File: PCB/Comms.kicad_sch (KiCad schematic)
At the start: 19 parts, among them J2 USB_In, J3 Trackpad, J4 OLED, U4 PMW3360DM-T2QU, U5 SRV05-4

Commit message: Rewording of readme. Added files for JLC PCBA. Changed USB C connector and moved it away from board.
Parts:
- C20: LCSC (none) -> C14663; LCSC part number C14663 -> (none)
- C93: LCSC (none) -> C19666; LCSC part number C19666 -> (none)
- C94: LCSC (none) -> C1525; LCSC part number C1525 -> (none)
- D64: LCSC (none) -> C193402; LCSC part number C193402 -> (none)
- D65, D66: LCSC (none) -> C8598; LCSC part number C8598 -> (none)
- F1: LCSC (none) -> C66453; LCSC part number C66453 -> (none)
- J2: footprint Honeydew:HRO-TYPE-C-31-M-13x -> Honeydew:HRO-TYPE-C-31-M-12; LCSC (none) -> C165948; LCSC part number C2848620 -> (none)
- J3: LCSC (none) -> C88360; LCSC part number C88360 -> (none)
- R10, R14: LCSC (none) -> C25744; LCSC part number C25744 -> (none)
- R11: LCSC (none) -> C25164; LCSC part number C25164 -> (none)
- R12, R13: LCSC (none) -> C25905; LCSC part number C25905 -> (none)
- R26: LCSC (none) -> C23138; LCSC part number C23138 -> (none)
- U4: now left out of the parts list
- U5: LCSC (none) -> C85364; LCSC part number C85364 -> (none)
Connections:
- net at J2.A5 (CC1): now also R13.2; no longer R12.2
- net at J2.B5 (CC2): now also R12.2; no longer R13.2
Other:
- moved on the sheet: R12, R13
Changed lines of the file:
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@@
-      (effects (font (size 1.27 1.27)) hide)
-    )
-    (property "LCSC part number" "C8598" (at 85.09 21.59 0)
       (effects (font (size 1.27 1.27)) hide)
     )
     (property "Description" "SOD-123 schottky" (at 85.09 21.59 0)
+      (effects (font (size 1.27 1.27)) hide)
+    )
+    (property "LCSC" "C8598" (at 85.09 21.59 0)
       (effects (font (size 1.27 1.27)) hide)
     )
@@
       (effects (font (size 1.27 1.27)) hide)
     )
-    (property "LCSC part number" "C88360" (at 116.84 83.82 0)
-      (effects (font (size 1.27 1.27)) hide)
-    )
     (property "Description" "12-pin FFC/FPC connector" (at 116.84 83.82 0)
+      (effects (font (size 1.27 1.27)) hide)
+    )
+    (property "LCSC" "C88360" (at 116.84 83.82 0)
       (effects (font (size 1.27 1.27)) hide)
     )
@@
       (effects (font (size 1.27 1.27)) hide)
     )
-    (property "LCSC part number" "C25744" (at 118.11 29.21 0)
+    (property "LCSC" "C25744" (at 118.11 29.21 0)
       (effects (font (size 1.27 1.27)) hide)
     )
@@
       (effects (font (size 1.27 1.27)) hide)
     )
-    (property "LCSC part number" "C14663" (at 24.13 67.31 0)
-      (effects (font (size 1.27 1.27)) hide)
-    )
     (property "Description" "0603 capacitor" (at 24.13 67.31 0)
+      (effects (font (size 1.27 1.27)) hide)
+    )
+    (property "LCSC" "C14663" (at 24.13 67.31 0)
       (effects (font (size 1.27 1.27)) hide)
     )
@@
       (effects (font (size 1.27 1.27)))
     )
-    (property "Footprint" "Honeydew:HRO-TYPE-C-31-M-13x" (at 30.48 36.83 0)
+    (property "Footprint" "Honeydew:HRO-TYPE-C-31-M-12" (at 30.48 36.83 0)
       (effects (font (size 1.27 1.27)) hide)
     )
@@
       (effects (font (size 1.27 1.27)) hide)
     )
-    (property "LCSC part number" "C2848620" (at 26.67 36.83 0)
-      (effects (font (size 1.27 1.27)) hide)
-    )
     (property "Description" "USB C 2.0 jack" (at 26.67 36.83 0)
       (effects (font (size 1.27 1.27)) hide)
     )
-    (property "LCSC" "" (at 26.67 36.83 0)
+    (property "LCSC" "C165948" (at 26.67 36.83 0)
       (effects (font (size 1.27 1.27)) hide)
     )
@@
       (effects (font (size 1.27 1.27)) hide)
     )
-    (property "LCSC part number" "C25164" (at 125.73 29.21 0)
-      (effects (font (size 1.27 1.27)) hide)
-    )
     (property "Description" "0402 resistor" (at 125.73 29.21 0)
       (effects (font (size 1.27 1.27)) hide)
     )
+    (property "LCSC" "C25164" (at 125.73 29.21 0)
+      (effects (font (size 1.27 1.27)) hide)
+    )
     (pin "1")
     (pin "2")
@@
   )
   (symbol (lib_name "PMW3360DM-T2QU_1") (lib_id "Ogen:PMW3360DM-T2QU") (at 140.97 39.37 0) (unit 1)
-    (in_bom yes) (on_board yes) (dnp no) (fields_autoplaced)
+    (in_bom no) (on_board yes) (dnp no) (fields_autoplaced)
     (property "Reference" "U4" (at 152.1402 54.61 0)
       (effects (font (size 1.27 1.27)))
@@
     )
     (property "Description" "Optical sensor" (at 140.97 39.37 0)
+      (effects (font (size 1.27 1.27)) hide)
+    )
+    (property "LCSC" "" (at 140.97 39.37 0)
       (effects (font (size 1.27 1.27)) hide)
     )
@@
       (effects (font (size 1.27 1.27)) hide)
     )
-    (property "LCSC part number" "C19666" (at 148.59 19.05 0)
-      (effects (font (size 1.27 1.27)) hide)
-    )
     (property "Description" "0603 capacitor" (at 148.59 19.05 0)
+      (effects (font (size 1.27 1.27)) hide)
+    )
+    (property "LCSC" "C19666" (at 148.59 19.05 0)
       (effects (font (size 1.27 1.27)) hide)
     )
@@
       (effects (font (size 1.27 1.27)) hide)
     )
-    (property "LCSC" "" (at 77.47 21.59 90)
-      (effects (font (size 1.27 1.27)) hide)
-    )
-    (property "LCSC part number" "C66453" (at 77.47 21.59 0)
-      (effects (font (size 1.27 1.27)) hide)
-    )
     (property "Description" "1206 fuse 1A" (at 77.47 21.59 0)
+      (effects (font (size 1.27 1.27)) hide)
+    )
+    (property "LCSC" "C66453" (at 77.47 21.59 0)
       (effects (font (size 1.27 1.27)) hide)
     )
@@
       (effects (font (size 1.27 1.27)) hide)
     )
-    (property "LCSC part number" "C85364" (at 72.39 44.45 0)
-      (effects (font (size 1.27 1.27)) hide)
-    )
     (property "Description" "SOT-26 ESD protector" (at 72.39 44.45 0)
       (effects (font (size 1.27 1.27)) hide)
     )
-    (property "LCSC" "" (at 72.39 44.45 0)
+    (property "LCSC" "C85364" (at 72.39 44.45 0)
       (effects (font (size 1.27 1.27)) hide)
     )
@@
       (effects (font (size 1.27 1.27)) hide)
     )
+    (property "LCSC" "" (at 166.37 35.56 0)
+      (effects (font (size 1.27 1.27)) hide)
+    )
     (pin "1")
     (pin "2")
@@
     )
   )
-  (symbol (lib_id "Device:R_Small") (at 46.99 26.67 270) (unit 1)
-    (in_bom yes) (on_board yes) (dnp no)
-    (property "Reference" "R12" (at 45.72 24.13 90)
+  (symbol (lib_id "Device:R_Small") (at 46.99 29.21 270) (mirror x) (unit 1)
+    (in_bom yes) (on_board yes) (dnp no)
+    (property "Reference" "R12" (at 45.72 31.75 90)
       (effects (font (size 1.27 1.27)) (justify right))
     )
-    (property "Value" "5k1" (at 48.26 24.13 90)
-      (effects (font (size 1.27 1.27)) (justify left))
-    )
-    (property "Footprint" "Resistor_SMD:R_0402_1005Metric" (at 46.99 26.67 0)
-      (effects (font (size 1.27 1.27)) hide)
-    )
-    (property "Datasheet" "~" (at 46.99 26.67 0)
-      (effects (font (size 1.27 1.27)) hide)
-    )
-    (property "LCSC part number" "C25905" (at 46.99 26.67 0)
-      (effects (font (size 1.27 1.27)) hide)
-    )
-    (property "Description" "0402 resistor" (at 46.99 26.67 0)
+    (property "Value" "5k1" (at 48.26 31.75 90)
+      (effects (font (size 1.27 1.27)) (justify left))
+    )
+    (property "Footprint" "Resistor_SMD:R_0402_1005Metric" (at 46.99 29.21 0)
+      (effects (font (size 1.27 1.27)) hide)
+    )
+    (property "Datasheet" "~" (at 46.99 29.21 0)
+      (effects (font (size 1.27 1.27)) hide)
+    )
+    (property "Description" "0402 resistor" (at 46.99 29.21 0)
+      (effects (font (size 1.27 1.27)) hide)
+    )
+    (property "LCSC" "C25905" (at 46.99 29.21 0)
       (effects (font (size 1.27 1.27)) hide)
     )
@@
       (effects (font (size 1.27 1.27)) hide)
     )
-    (property "LCSC part number" "C23138" (at 19.05 67.31 0)
-      (effects (font (size 1.27 1.27)) hide)
-    )
     (property "Description" "0603 resistor" (at 19.05 67.31 0)
+      (effects (font (size 1.27 1.27)) hide)
+    )
+    (property "LCSC" "C23138" (at 19.05 67.31 0)
       (effects (font (size 1.27 1.27)) hide)
     )
@@
       (effects (font (size 1.27 1.27)) hide)
     )
-    (property "LCSC part number" "C25744" (at 166.37 26.67 0)
+    (property "LCSC" "C25744" (at 166.37 26.67 0)
       (effects (font (size 1.27 1.27)) hide)
     )
@@
     )
   )
-  (symbol (lib_id "Device:R_Small") (at 46.99 29.21 270) (mirror x) (unit 1)
-    (in_bom yes) (on_board yes) (dnp no)
-    (property "Reference" "R13" (at 45.72 31.75 90)
+  (symbol (lib_id "Device:R_Small") (at 46.99 26.67 270) (unit 1)
+    (in_bom yes) (on_board yes) (dnp no)
+    (property "Reference" "R13" (at 45.72 24.13 90)
       (effects (font (size 1.27 1.27)) (justify right))
     )
-    (property "Value" "5k1" (at 48.26 31.75 90)
-      (effects (font (size 1.27 1.27)) (justify left))
-    )
-    (property "Footprint" "Resistor_SMD:R_0402_1005Metric" (at 46.99 29.21 0)
-      (effects (font (size 1.27 1.27)) hide)
-    )
-    (property "Datasheet" "~" (at 46.99 29.21 0)
-      (effects (font (size 1.27 1.27)) hide)
-    )
-    (property "LCSC part number" "C25905" (at 46.99 29.21 0)
-      (effects (font (size 1.27 1.27)) hide)
-    )
-    (property "Description" "0402 resistor" (at 46.99 29.21 0)
+    (property "Value" "5k1" (at 48.26 24.13 90)
+      (effects (font (size 1.27 1.27)) (justify left))
+    )
+    (property "Footprint" "Resistor_SMD:R_0402_1005Metric" (at 46.99 26.67 0)
+      (effects (font (size 1.27 1.27)) hide)
+    )
+    (property "Datasheet" "~" (at 46.99 26.67 0)
+      (effects (font (size 1.27 1.27)) hide)
+    )
+    (property "Description" "0402 resistor" (at 46.99 26.67 0)
+      (effects (font (size 1.27 1.27)) hide)
+    )
+    (property "LCSC" "C25905" (at 46.99 26.67 0)
       (effects (font (size 1.27 1.27)) hide)
     )
@@
       (effects (font (size 1.27 1.27)) hide)
     )
-    (property "LCSC part number" "C8598" (at 72.39 26.67 0)
-      (effects (font (size 1.27 1.27)) hide)
-    )
     (property "Description" "SOD-123 schottky" (at 72.39 26.67 0)
+      (effects (font (size 1.27 1.27)) hide)
+    )
+    (property "LCSC" "C8598" (at 72.39 26.67 0)
       (effects (font (size 1.27 1.27)) hide)
     )
@@
       (effects (font (size 1.27 1.27)) hide)
     )
-    (property "LCSC part number" "C193402" (at 57.15 26.67 0)
-      (effects (font (size 1.27 1.27)) hide)
-    )
     (property "Description" "SOD-123 TVS" (at 57.15 26.67 0)
+      (effects (font (size 1.27 1.27)) hide)
+    )
+    (property "LCSC" "C193402" (at 57.15 26.67 0)
       (effects (font (size 1.27 1.27)) hide)
     )
@@
       (effects (font (size 1.27 1.27)) hide)
     )
-    (property "LCSC part number" "C1525" (at 148.59 24.13 0)
-      (effects (font (size 1.27 1.27)) hide)
-    )
     (property "Description" "0402 capacitor" (at 148.59 24.13 0)
+      (effects (font (size 1.27 1.27)) hide)
+    )
+    (property "LCSC" "C1525" (at 148.59 24.13 0)
       (effects (font (size 1.27 1.27)) hide)
     )
@@
       (effects (font (size 1.27 1.27)) hide)
     )
-    (property "LCSC part number" "" (at 146.05 76.2 0)
-      (effects (font (size 1.27 1.27)) hide)
-    )
     (property "Description" "SSD1315 OLED" (at 146.05 76.2 0)
       (effects (font (size 1.27 1.27)) hide)
     )
+    (property "LCSC" "" (at 146.05 76.2 0)
+      (effects (font (size 1.27 1.27)) hide)
+    )

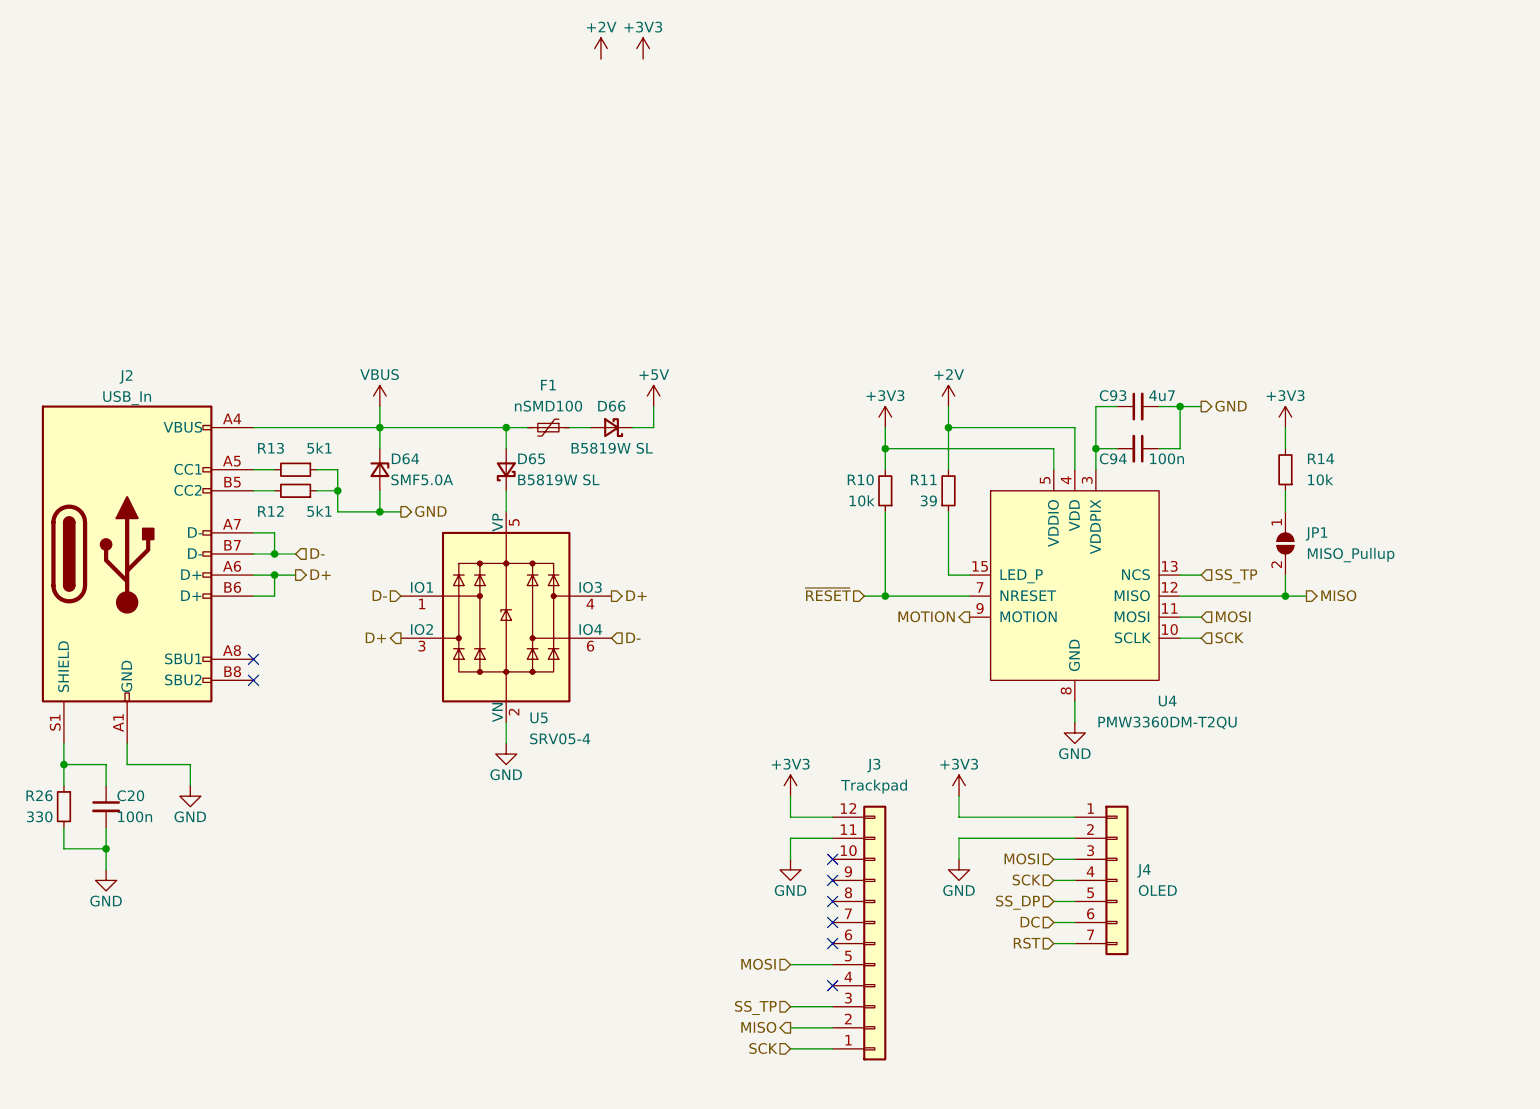
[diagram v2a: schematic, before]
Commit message: Added PH2.0 header for OLED. Changed plate to accommodate headers.
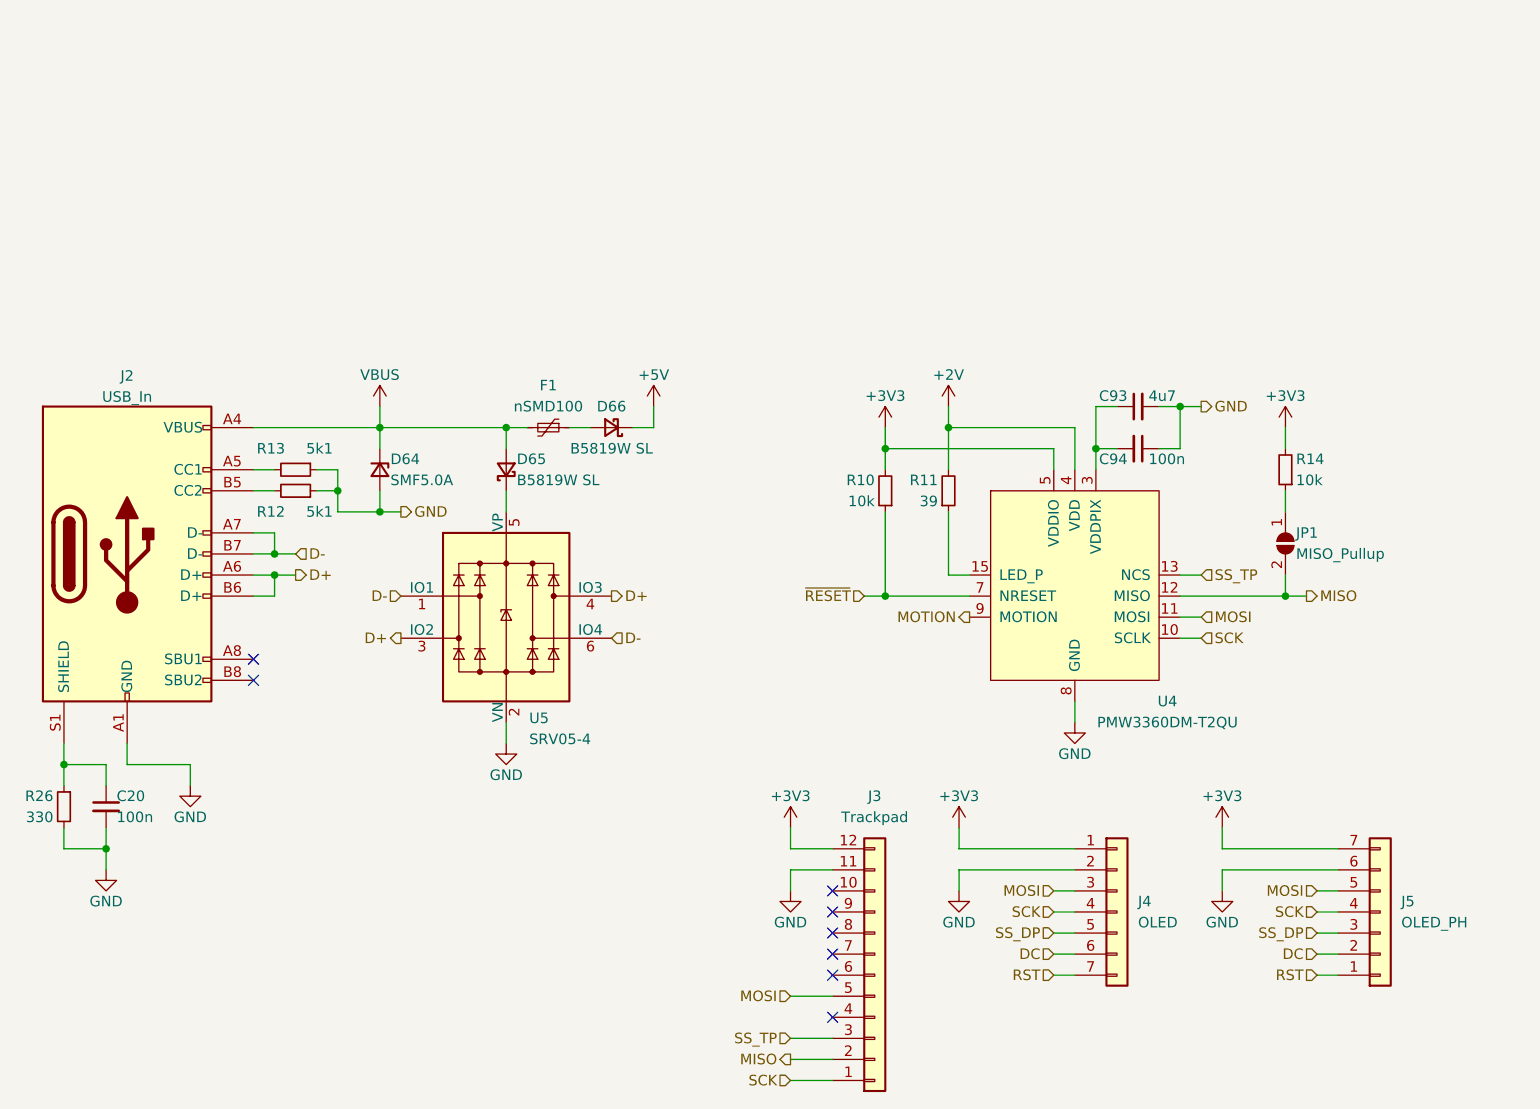
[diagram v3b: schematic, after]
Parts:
- added J5: OLED_PH, Connector_JST:JST_PH_S7B-PH-K_1x07_P2.00mm_Horizontal, symbol Connector_Generic:Conn_01x07
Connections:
- net +3V3: now also J5.7 (Pin_7)
- net DC: now also J5.2 (Pin_2)
- net GND: now also J5.6 (Pin_6)
- net MOSI: now also J5.5 (Pin_5)
- net RST: now also J5.1 (Pin_1)
- net SCK: now also J5.4 (Pin_4)
- net SS_DP: now also J5.3 (Pin_3)
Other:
- moved on the sheet: J3, J4

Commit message: V1.1 update.
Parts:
- removed C20: 100n, Capacitor_SMD:C_0603_1608Metric, symbol Device:C_Small
- removed R26: 330, Resistor_SMD:R_0603_1608Metric, symbol Device:R_Small
- added FB1: GZ2012D601TF, Inductor_SMD:L_0805_2012Metric, symbol Device:FerriteBead_Small
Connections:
- net GND: now also FB1.2
- net at J2.S1 (SHIELD): now also FB1.1

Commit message: Added level shifter to the RGB signal, just in case.
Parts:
- FB1: value GZ2012D601TF -> 60R@100MHz; footprint Inductor_SMD:L_0805_2012Metric -> Inductor_SMD:L_1206_3216Metric; LCSC C1017 -> C33600
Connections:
- net MOTION: now also J3.4 (Pin_4)
- net RST renamed RST_OLED
- net SS_DP renamed SS_OLED
- net SS_TP renamed SS_TB
- net ~{RESET} renamed ~{RST}_TB
- no-connect marks 8 -> 7
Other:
- moved on the sheet: J4, J5

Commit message: More V1.1 updates
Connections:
- net ~{RST}_TB is gone; now on net ~{RST}: R10.1, U4.7 (NRESET)
- net DC renamed DC_OLED
- net RST_OLED renamed ~{RST}
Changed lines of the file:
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@@
   (title_block
     (title "Honeydew unsplit ergonomic keyboard")
-    (date "2023-03-18")
+    (date "2023-03-31")
     (rev "V1.1")
   )
@@
     (stroke (width 0) (type default))
   )
-  (hierarchical_label "RST_OLED" (shape input) (at 175.26 87.63 180) (fields_autoplaced)
-    (effects (font (size 1.27 1.27)) (justify right))
-  )
   (hierarchical_label "D-" (shape input) (at 59.69 41.91 180) (fields_autoplaced)
     (effects (font (size 1.27 1.27)) (justify right))
@@
     (effects (font (size 1.27 1.27)) (justify right))
   )
+  (hierarchical_label "DC_OLED" (shape input) (at 175.26 85.09 180) (fields_autoplaced)
+    (effects (font (size 1.27 1.27)) (justify right))
+  )
   (hierarchical_label "SS_TB" (shape input) (at 106.68 95.25 180) (fields_autoplaced)
     (effects (font (size 1.27 1.27)) (justify right))
   )
-  (hierarchical_label "RST_OLED" (shape input) (at 140.97 87.63 180) (fields_autoplaced)
+  (hierarchical_label "~{RST}" (shape input) (at 140.97 87.63 180) (fields_autoplaced)
     (effects (font (size 1.27 1.27)) (justify right))
   )
@@
     (effects (font (size 1.27 1.27)) (justify left))
   )
+  (hierarchical_label "~{RST}" (shape input) (at 175.26 87.63 180) (fields_autoplaced)
+    (effects (font (size 1.27 1.27)) (justify right))
+  )
   (hierarchical_label "SS_OLED" (shape input) (at 175.26 82.55 180) (fields_autoplaced)
     (effects (font (size 1.27 1.27)) (justify right))
@@
     (effects (font (size 1.27 1.27)) (justify right))
   )
-  (hierarchical_label "DC" (shape input) (at 140.97 85.09 180) (fields_autoplaced)
+  (hierarchical_label "DC_OLED" (shape input) (at 140.97 85.09 180) (fields_autoplaced)
     (effects (font (size 1.27 1.27)) (justify right))
   )
@@
     (effects (font (size 1.27 1.27)) (justify right))
   )
-  (hierarchical_label "DC" (shape input) (at 175.26 85.09 180) (fields_autoplaced)
-    (effects (font (size 1.27 1.27)) (justify right))
-  )
-  (hierarchical_label "~{RST}_TB" (shape input) (at 115.57 41.91 180) (fields_autoplaced)
-    (effects (font (size 1.27 1.27)) (justify right))
-  )
+  (hierarchical_label "~{RST}" (shape input) (at 115.57 41.91 180) (fields_autoplaced)
+    (effects (font (size 1.27 1.27)) (justify right))
+  )
